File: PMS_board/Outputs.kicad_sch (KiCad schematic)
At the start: 37 parts, among them U1 VN7140ASTR, U11 VN7007AHTR, U2 VN7140ASTR, U23 VN7007AHTR, U8 VN7140ASTR

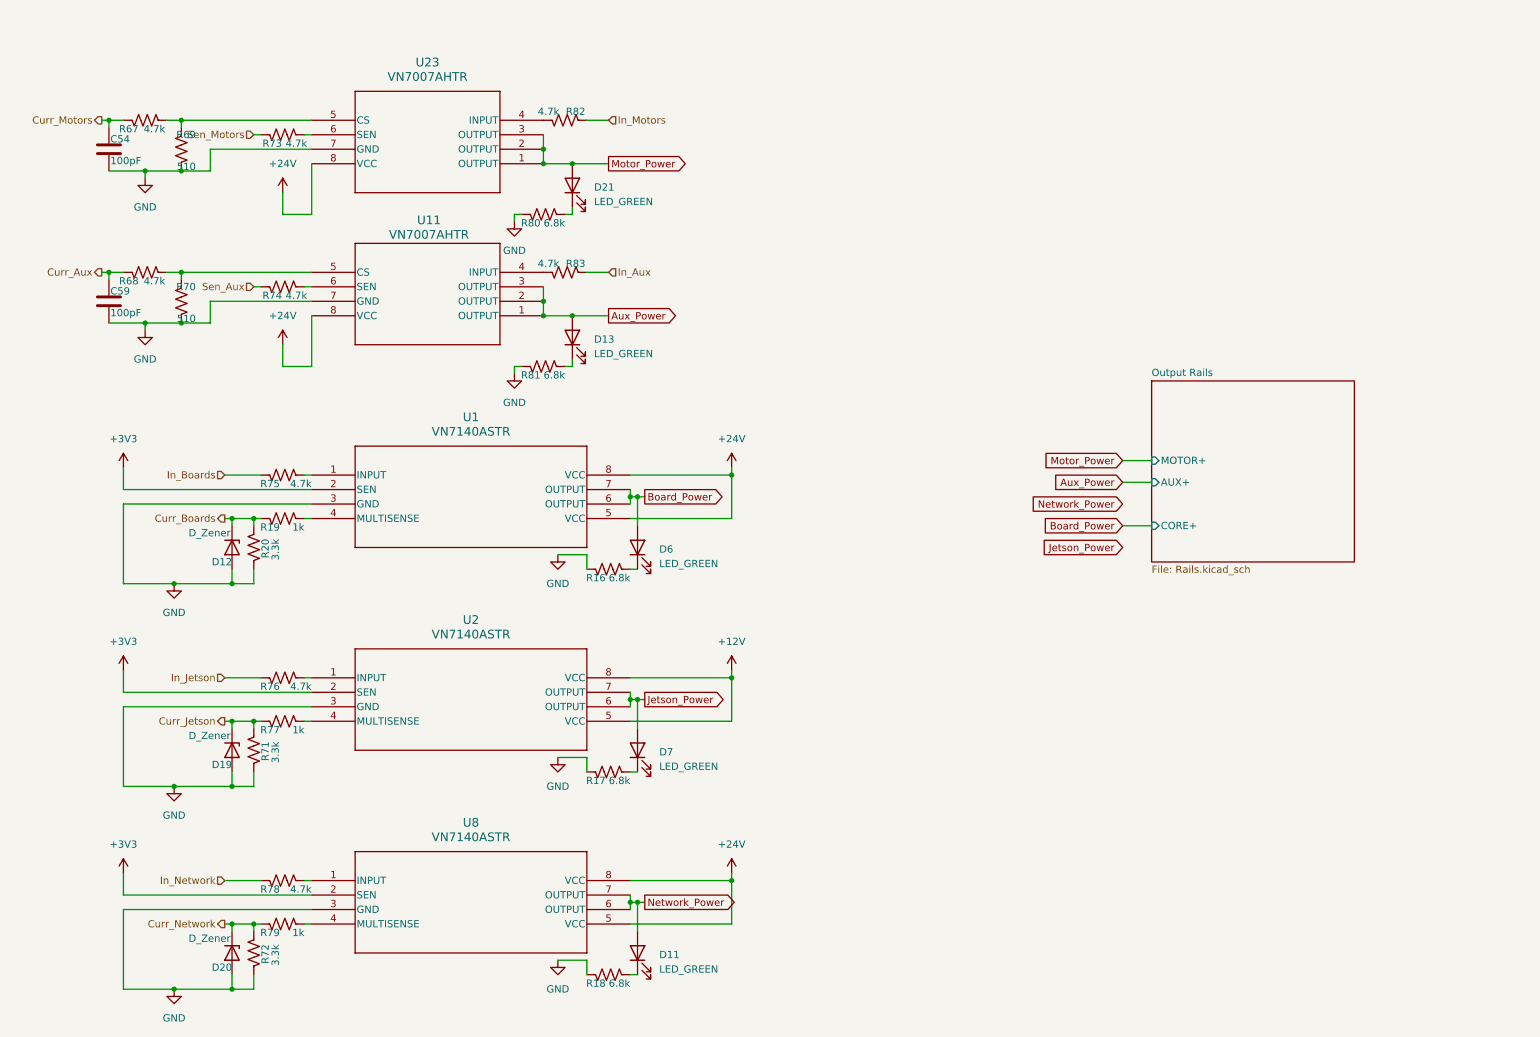
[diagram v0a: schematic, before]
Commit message: Add reverse voltage protection
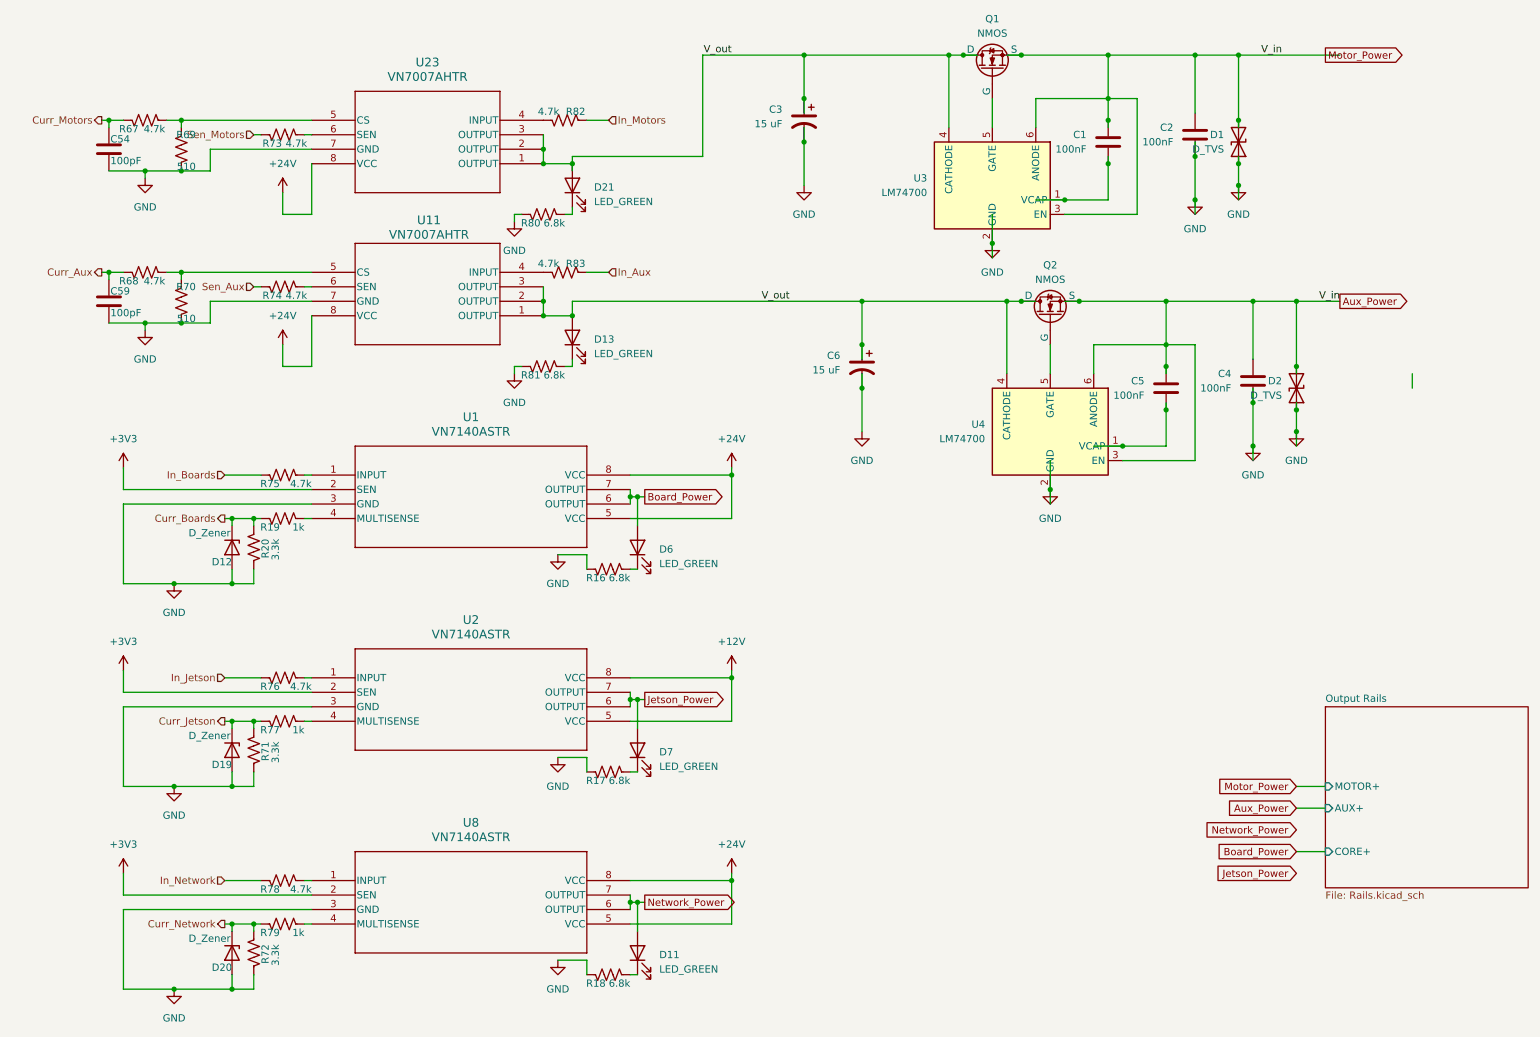
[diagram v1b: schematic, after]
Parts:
- added C1, C5: 100nF, Package_SON:WSON-6-1EP_2x2mm_P0.65mm_EP1x1.6mm, symbol Device:C
- added C2, C4: 100nF, symbol Device:C
- added C3, C6: 15 uF, symbol Device:C_Polarized_US
- added D1, D2: D_TVS, Package_SON:WSON-8-1EP_6x5mm_P1.27mm_EP3.4x4mm, symbol Device:D_TVS
- added Q1, Q2: NMOS, Package_DFN_QFN:Nordic_AQFN-94-1EP_7x7mm_P0.4mm, symbol Simulation_SPICE:NMOS
- added U3, U4: LM74700, Package_TO_SOT_SMD:SOT-23-6, symbol Power_Management:LM74700
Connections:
- net Aux_Power: now also C1.1, C2.1, C4.1, C5.1, D1.2 (A2), D2.2 (A2), Q1.3 (S), Q2.3 (S), U3.3 (EN), U3.6 (ANODE), U4.3 (EN), U4.6 (ANODE); no longer D13.2 (A), U11.1 (OUTPUT), U11.2 (OUTPUT), U11.3 (OUTPUT)
- net GND: now also C2.2, C3.2, C4.2, C6.2, D1.1 (A1), D2.1 (A1), U3.2 (GND), U4.2 (GND)
- net Motor_Power renamed V_out
- net V_out: now also D13.2 (A), U11.1 (OUTPUT), U11.2 (OUTPUT), U11.3 (OUTPUT), C3.1, C6.1, Q1.1 (D), Q2.1 (D), U3.4 (CATHODE), U4.4 (CATHODE)
- new net: C5.2, U4.1 (VCAP)
- new net: C1.2, U3.1 (VCAP)
- new net: Q1.2 (G), U3.5 (GATE)
- new net: Q2.2 (G), U4.5 (GATE)

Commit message: Finish Schematic
There's definitely stuff I missed, but I'm tired so we can review later. For my members to keep track of things, these are the changes/last minute additions I ran out of time to teach:
- brake chopper circuitry & reverse voltage protection for aux & motor rails
- microcontroller pinnouts
- net connections between sheets
- voltage resistors & system voltage measurements
- cell sense connectors & switch
- ADC routing
Please Please PLEASE ask questions about these additions. I don't want you guys to feel like you don't own this schematic, and I'm sorry I had to take away some of these designs to finish early. I definitely left too much on your plate to get everything perfect, which is my bad. I will happily walk through each and every circuit and help explain each part so you can better know your project when we get to reviewing and debugging later down the line.
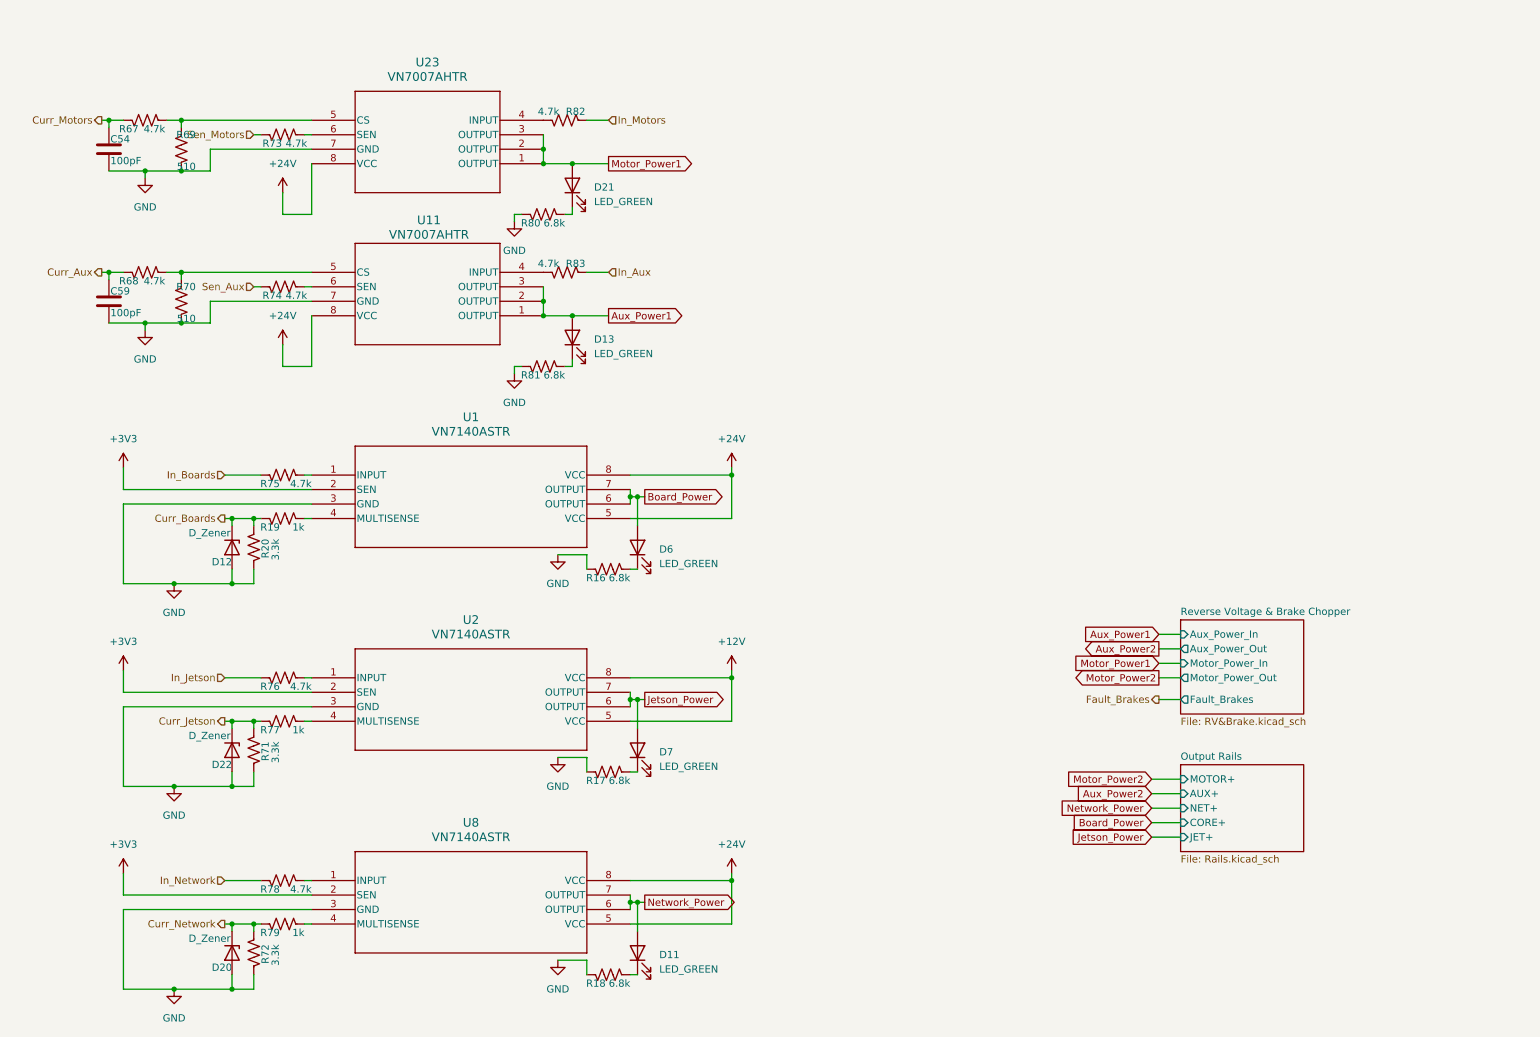
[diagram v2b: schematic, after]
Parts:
- removed C1, C5: 100nF, Package_SON:WSON-6-1EP_2x2mm_P0.65mm_EP1x1.6mm, symbol Device:C
- removed C2, C4: 100nF, symbol Device:C
- removed C3, C6: 15 uF, symbol Device:C_Polarized_US
- removed D1, D2: D_TVS, Package_SON:WSON-8-1EP_6x5mm_P1.27mm_EP3.4x4mm, symbol Device:D_TVS
- removed D19: D_Zener, Diode_SMD:Littelfuse_PolyZen-LS, symbol Device:D_Zener
- removed Q1, Q2: NMOS, Package_DFN_QFN:Nordic_AQFN-94-1EP_7x7mm_P0.4mm, symbol Simulation_SPICE:NMOS
- removed U3, U4: LM74700, Package_TO_SOT_SMD:SOT-23-6, symbol Power_Management:LM74700
- added D22: D_Zener, Diode_SMD:Littelfuse_PolyZen-LS, symbol Device:D_Zener
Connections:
- net Curr_Jetson: now also D22.1 (K)
- net GND: now also D22.2 (A)
- net V_out renamed Aux_Power1
- net Aux_Power1: no longer D21.2 (A), U23.1 (OUTPUT), U23.2 (OUTPUT), U23.3 (OUTPUT)
- new net Motor_Power1: D21.2 (A), U23.1 (OUTPUT), U23.2 (OUTPUT), U23.3 (OUTPUT)
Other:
- added sheet Reverse Voltage & Brake Chopper (RV&Brake.kicad_sch)
- sheet Output Rails ports: added JET+, NET+; removed none

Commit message: Add Footprints & such
whoops forgot to push yesterday teehee
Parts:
- C54, C59: footprint (none) -> Capacitor_SMD:C_0603_1608Metric
- U1, U2, U8: footprint SO-8_STM -> VN7140ASTR:SO-8_STM
- U11, U23: footprint OCTOPAK_STM -> VN7007AHTR:OCTOPAK_STM
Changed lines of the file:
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@@
 			)
 		)
-		(property "Footprint" ""
+		(property "Footprint" "Capacitor_SMD:C_0603_1608Metric"
 			(at 29.5148 57.15 0)
 			(hide yes)
@@
 			)
 		)
-		(property "Footprint" "SO-8_STM"
+		(property "Footprint" "VN7140ASTR:SO-8_STM"
 			(at 66.04 127 0)
 			(hide yes)
@@
 			)
 		)
-		(property "Footprint" "OCTOPAK_STM"
+		(property "Footprint" "VN7007AHTR:OCTOPAK_STM"
 			(at 106.68 63.5 0)
 			(hide yes)
@@
 			)
 		)
-		(property "Footprint" "SO-8_STM"
+		(property "Footprint" "VN7140ASTR:SO-8_STM"
 			(at 66.04 162.56 0)
 			(hide yes)
@@
 			)
 		)
-		(property "Footprint" "SO-8_STM"
+		(property "Footprint" "VN7140ASTR:SO-8_STM"
 			(at 66.04 91.44 0)
 			(hide yes)
@@
 			)
 		)
-		(property "Footprint" ""
+		(property "Footprint" "Capacitor_SMD:C_0603_1608Metric"
 			(at 29.5148 30.48 0)
 			(hide yes)
@@
 			)
 		)
-		(property "Footprint" "OCTOPAK_STM"
+		(property "Footprint" "VN7007AHTR:OCTOPAK_STM"
 			(at 106.68 36.83 0)
 			(hide yes)

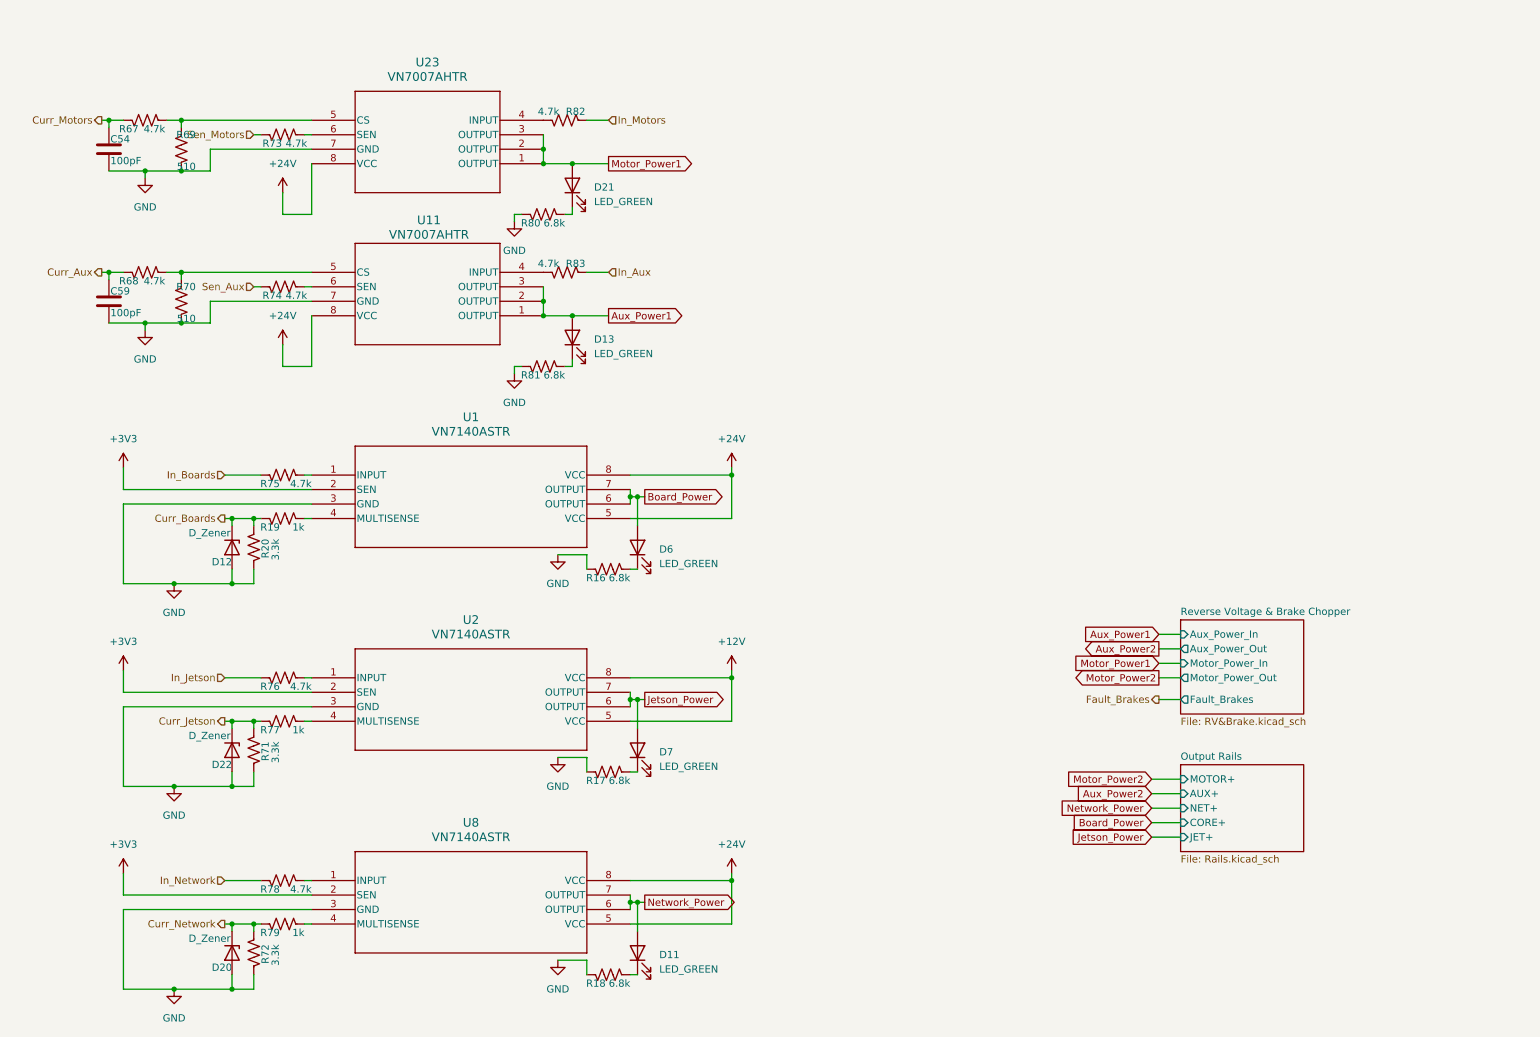
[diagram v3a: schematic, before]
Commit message: Minor component tweaks and added a seperate LED sheet
Changed component values
Added labels
Moved LEDs to it's own sheet
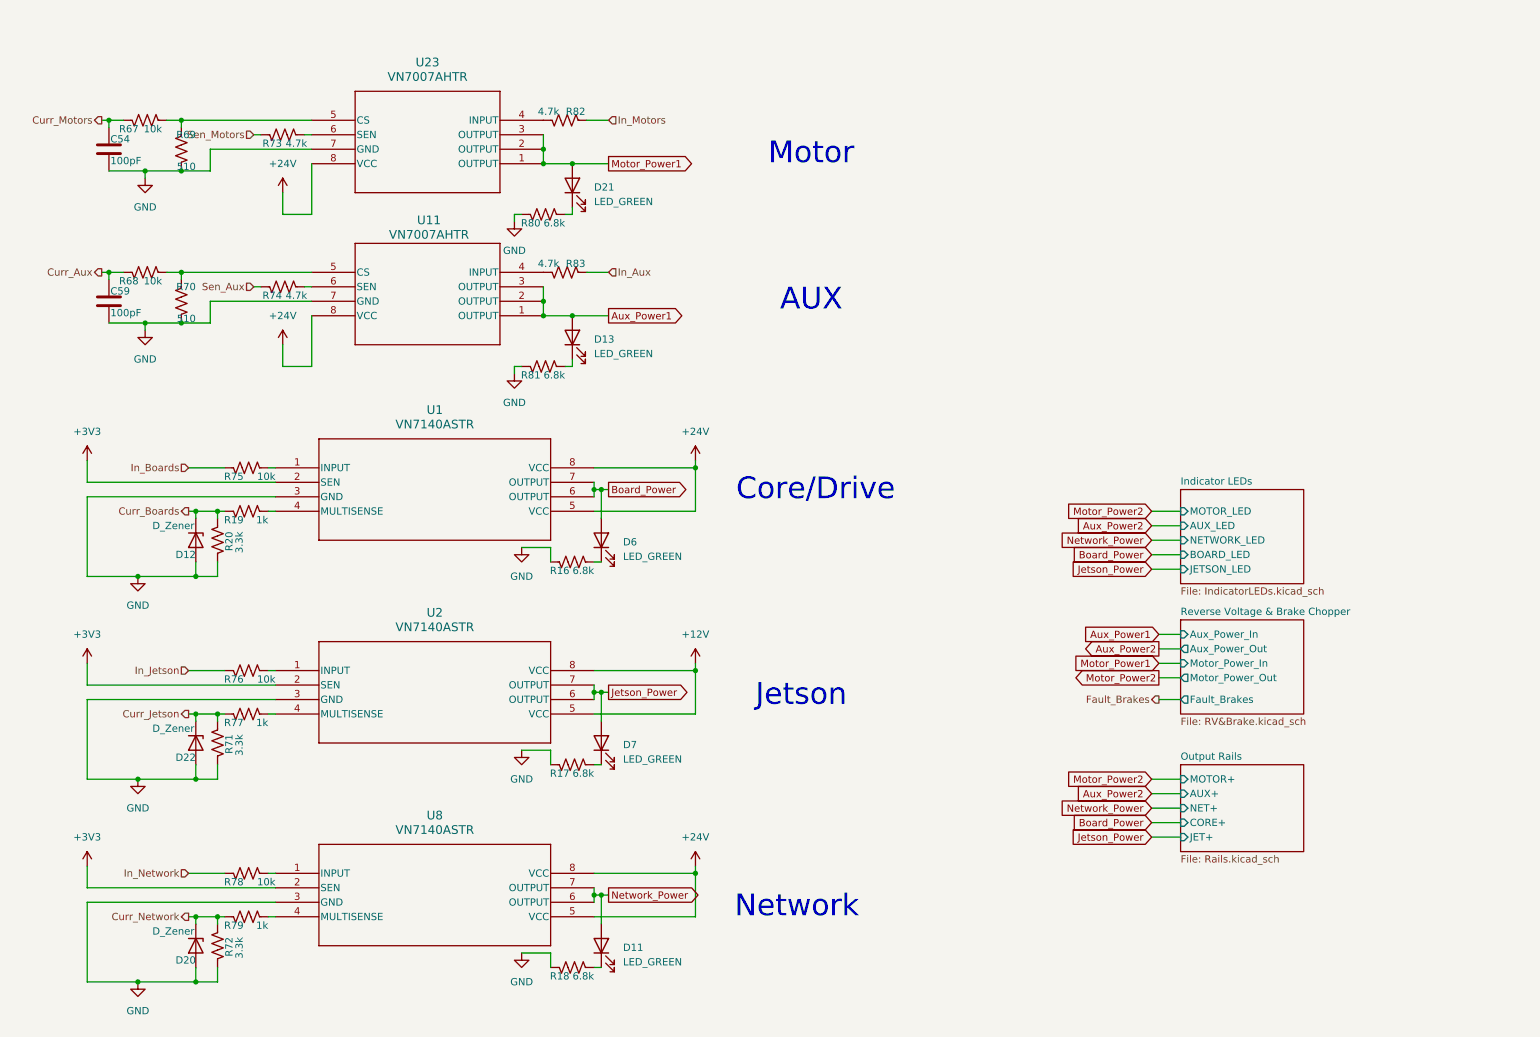
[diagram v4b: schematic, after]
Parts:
- R67, R68, R75, R76, R78: value 4.7k -> 10k
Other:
- added sheet Indicator LEDs (IndicatorLEDs.kicad_sch)
- note added: "AUX"
- note added: "Core/Drive"
- note added: "Jetson"
- note added: "Motor"
- note added: "Network"
- moved on the sheet: D11, D12, D20, D22, D6, D7, R16, R17, R18, R19, R20, R71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
